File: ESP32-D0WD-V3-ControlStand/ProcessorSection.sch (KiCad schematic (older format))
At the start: 31 parts

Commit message: Nearly complete schematic.  Added Antenna footprint.
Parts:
- removed J?: Programming Header, Pin_Headers:Pin_Header_Straight_2x03_Pitch2.54mm, symbol Conn_02x03_Odd_Even
- added AE?: Antenna_Shield, Antenna:Antenna, symbol Antenna_Shield
- added C? (x2): 270pf, Capacitors_SMD:C_0402, symbol C_Small
- added C? (x2): 47pf, Capacitors_SMD:C_0402, symbol C_Small
- added C?: 10pf, Capacitors_SMD:C_0402, symbol C_Small
- added C? (x2): 100nf, Capacitors_SMD:C_0402, symbol C_Small
- added C?: 4.7uf, Capacitors_SMD:CP_Elec_4x5.7, symbol CP1_Small
- added C?: 5.8pf, Capacitors_SMD:C_0402, symbol C_Small
- added J?: USB_OTG, Connectors_USB:USB_Micro-B_Molex_47346-0001, symbol USB_OTG
- added L? (x2): Ferrite Bead, Inductors_SMD:L_0402, symbol Ferrite_Bead_Small
- added Q? (x2): UMH3N, TO_SOT_Packages_SMD:SOT-363_SC-70-6, symbol UMH3N
- added R? (x2): 27, Resistors_SMD:R_0402, symbol R
- added U?: FT231XS-R, Housings_SSOP:SSOP-20_5.3x7.2mm_Pitch0.65mm, symbol FT231XS-R
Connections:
- net labels added: 0, 12, 16, 17, 18, 19, 23, 25, 26, 27, 32, 33, 34, 35, Antenna, DTR, RTS, Reset, VBUS, VN, VP
- net labels removed: GPIO0(Buttons1), GPIO12(Points1), GPIO13(Points2), GPIO14(Points3), GPIO16(Buttons4), GPIO17(LEDS1), GPIO18(LEDS2), GPIO19(LEDS3), GPIO23(LEDS4), GPIO25(Motor1), GPIO26(Motor2), GPIO27(Points4), GPIO32(Motor3), GPIO33(Motor4), GPIO34(OD1), GPIO35(OD2), GPIO36(OD3), GPIO37(Buttons3), GPIO38(Buttons2), GPIO39(OD4)
- wire segments 91 -> 140
- no-connect marks 1 -> 8

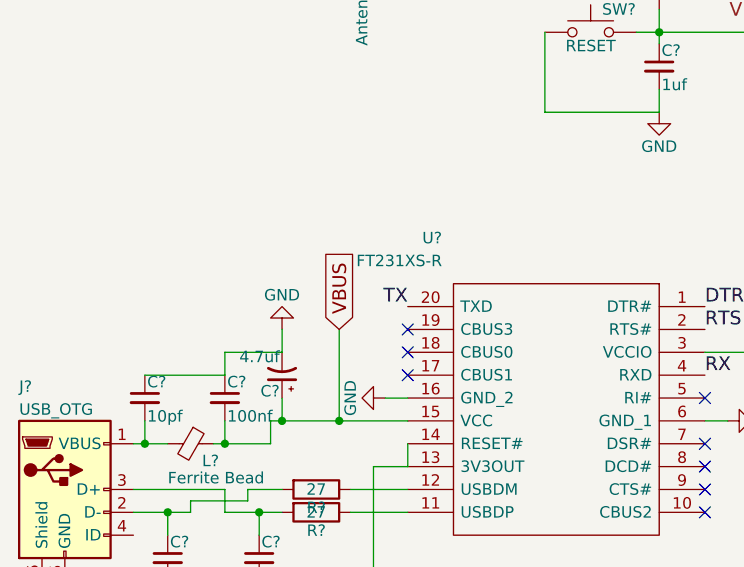
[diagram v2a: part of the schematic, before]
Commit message: Complete PS, work on parts spec.
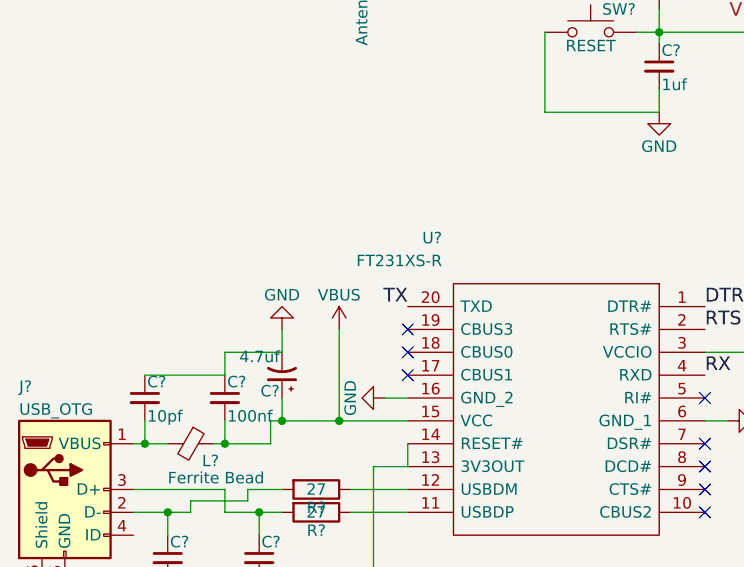
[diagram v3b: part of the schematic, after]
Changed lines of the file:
@@
 LIBS:ESP32-D0WD-V3
 LIBS:W25Q32JVSSIQ
+LIBS:mcp73871
+LIBS:lm2574n-5
 LIBS:ESP32-D0WD-V3-ControlStand-cache
 EELAYER 25 0
@@
 Wire Wire Line
 	3100 6850 3100 7000
-Text GLabel 2250 5300 1    60   Input ~ 0
-VBUS
 Wire Wire Line
 	2250 5300 2250 5700
@@
 Wire Wire Line
 	2650 3300 2650 3350
+$Comp
+L VBUS #PWR?
+U 1 1 62E2A6A1
+P 2250 5300
+F 0 "#PWR?" H 2250 5150 50  0001 C CNN
+F 1 "VBUS" H 2250 5450 50  0000 C CNN
+F 2 "" H 2250 5300 50  0001 C CNN
+F 3 "" H 2250 5300 50  0001 C CNN
+	1    2250 5300
+	1    0    0    -1
+$EndComp
 $EndSCHEMATC

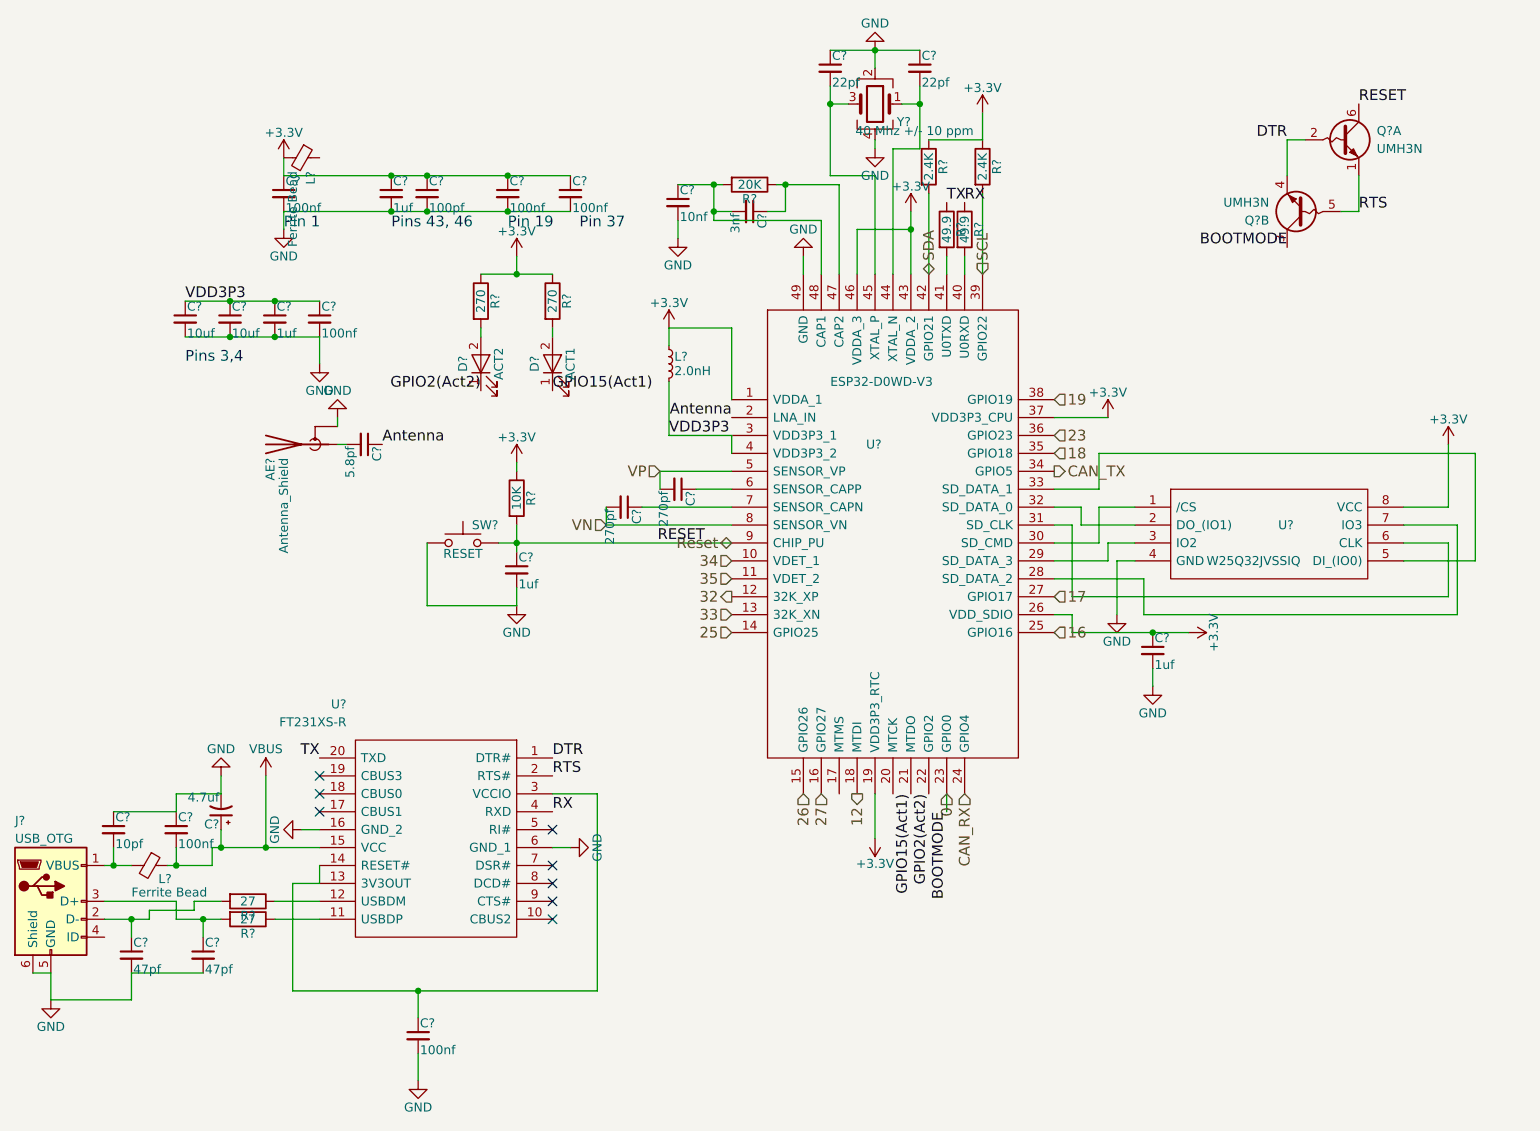
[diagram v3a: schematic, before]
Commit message: Completed parts spec for ESP32-D0WD-V3-ControlStand.
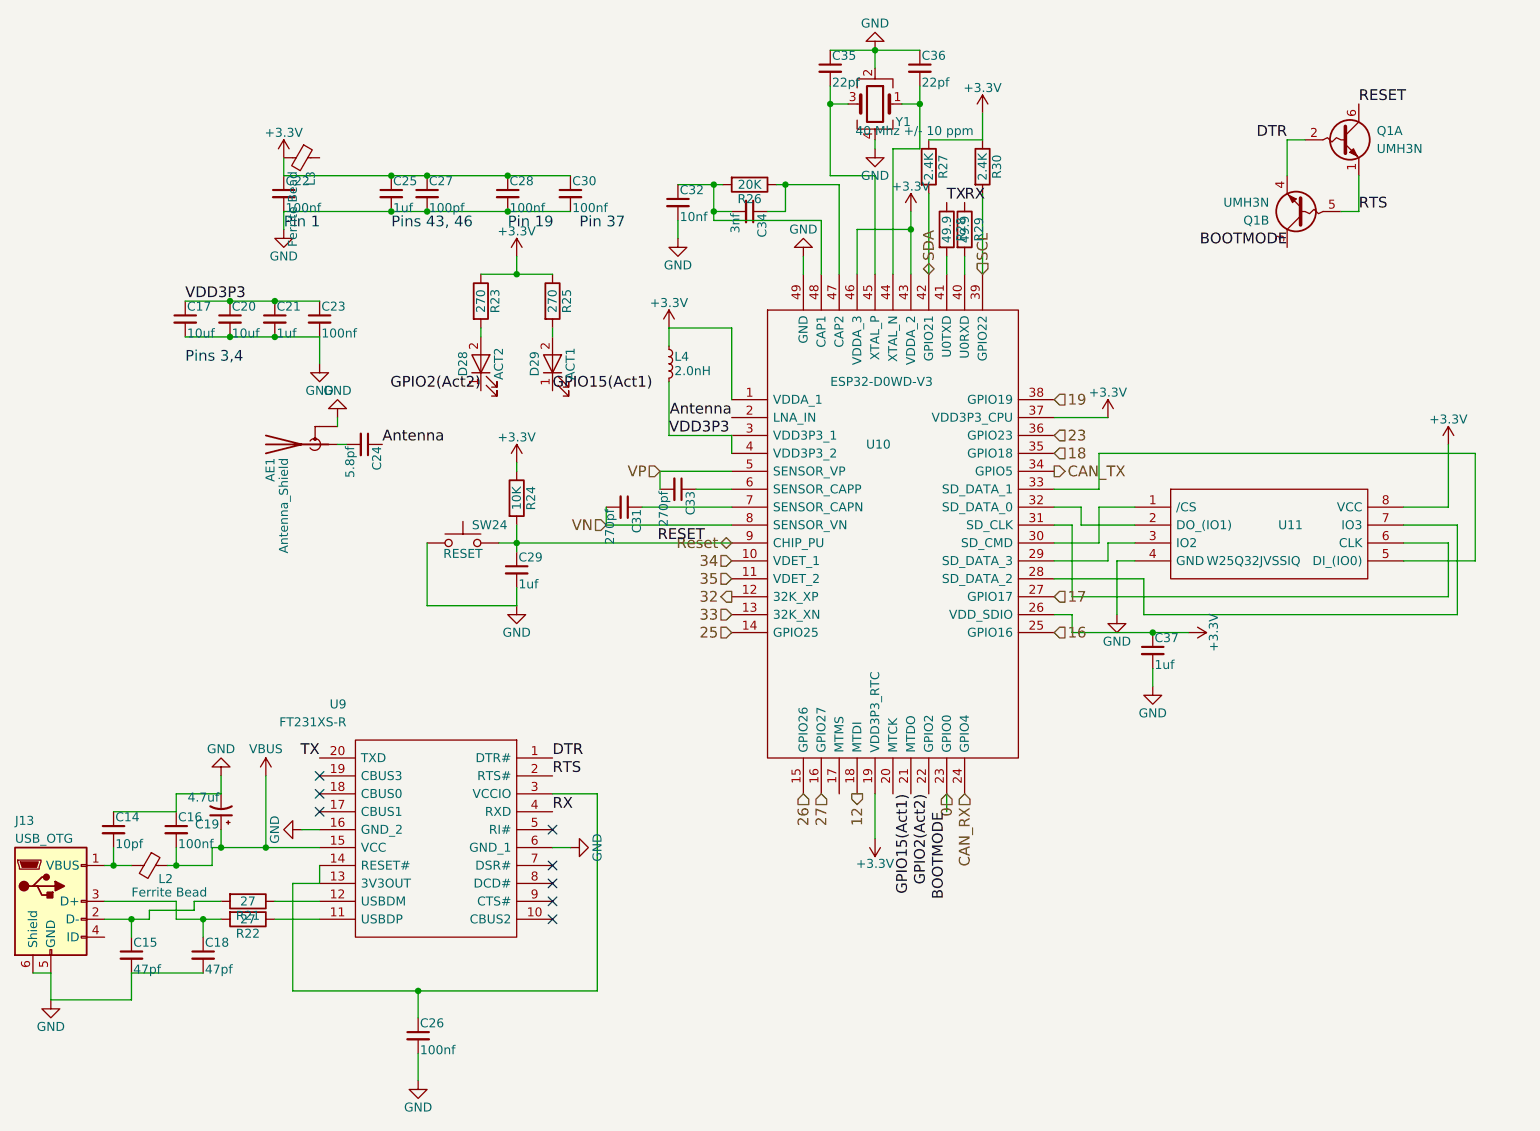
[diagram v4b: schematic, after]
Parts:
- gave numbers to parts that had none: 47

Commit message: Working on the PCB Layout.
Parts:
- removed L3: Ferrite Bead, Inductors_SMD:L_0402, symbol Ferrite_Bead_Small
- added MK17, MK18, MK19: Mounting_Hole, Mounting_Holes:MountingHole_2.5mm, symbol Mounting_Hole
- added MK20: Mounting_Hole_PAD, Mounting_Holes:MountingHole_2.5mm_Pad, symbol Mounting_Hole_PAD
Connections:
- no-connect marks 8 -> 9
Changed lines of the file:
@@
 LIBS:mcp73871
 LIBS:lm2574n-5
+LIBS:mechanical
+LIBS:graphic_symbols
 LIBS:ESP32-D0WD-V3-ControlStand-cache
 EELAYER 25 0
@@
 $EndComp
 $Comp
-L +3.3V #PWR85
+L +3.3V #PWR060
 U 1 1 62DF2387
 P 8850 3450
-F 0 "#PWR85" H 8850 3300 50  0001 C CNN
+F 0 "#PWR060" H 8850 3300 50  0001 C CNN
 F 1 "+3.3V" H 8850 3590 50  0000 C CNN
 F 2 "" H 8850 3450 50  0001 C CNN
@@
 $EndComp
 $Comp
-L GND #PWR82
+L GND #PWR061
 U 1 1 62DF2388
 P 7000 4400
-F 0 "#PWR82" H 7000 4150 50  0001 C CNN
+F 0 "#PWR061" H 7000 4150 50  0001 C CNN
 F 1 "GND" H 7000 4250 50  0000 C CNN
 F 2 "" H 7000 4400 50  0001 C CNN
@@
 $EndComp
 $Comp
-L GND #PWR71
+L GND #PWR062
 U 1 1 62DF2391
 P 3650 4350
-F 0 "#PWR71" H 3650 4100 50  0001 C CNN
+F 0 "#PWR062" H 3650 4100 50  0001 C CNN
 F 1 "GND" H 3650 4200 50  0000 C CNN
 F 2 "" H 3650 4350 50  0001 C CNN
@@
 $EndComp
 $Comp
-L +3.3V #PWR70
+L +3.3V #PWR063
 U 1 1 62DF2392
 P 3650 3550
-F 0 "#PWR70" H 3650 3400 50  0001 C CNN
+F 0 "#PWR063" H 3650 3400 50  0001 C CNN
 F 1 "+3.3V" H 3650 3690 50  0000 C CNN
 F 2 "" H 3650 3550 50  0001 C CNN
@@
 $EndComp
 $Comp
-L GND #PWR83
+L GND #PWR064
 U 1 1 62DF2394
 P 7200 4800
-F 0 "#PWR83" H 7200 4550 50  0001 C CNN
+F 0 "#PWR064" H 7200 4550 50  0001 C CNN
 F 1 "GND" H 7200 4650 50  0000 C CNN
 F 2 "" H 7200 4800 50  0001 C CNN
@@
 $EndComp
 $Comp
-L +3.3V #PWR84
+L +3.3V #PWR065
 U 1 1 62DF2395
 P 7400 4500
-F 0 "#PWR84" H 7400 4350 50  0001 C CNN
+F 0 "#PWR065" H 7400 4350 50  0001 C CNN
 F 1 "+3.3V" H 7400 4640 50  0000 C CNN
 F 2 "" H 7400 4500 50  0001 C CNN
@@
 $EndComp
 $Comp
-L +3.3V #PWR73
+L +3.3V #PWR066
 U 1 1 62DF2397
 P 4500 2800
-F 0 "#PWR73" H 4500 2650 50  0001 C CNN
+F 0 "#PWR066" H 4500 2650 50  0001 C CNN
 F 1 "+3.3V" H 4500 2940 50  0000 C CNN
 F 2 "" H 4500 2800 50  0001 C CNN
@@
 $EndComp
 $Comp
-L +3.3V #PWR81
+L +3.3V #PWR067
 U 1 1 62DF2398
 P 6950 3300
-F 0 "#PWR81" H 6950 3150 50  0001 C CNN
+F 0 "#PWR067" H 6950 3150 50  0001 C CNN
 F 1 "+3.3V" H 6950 3440 50  0000 C CNN
 F 2 "" H 6950 3300 50  0001 C CNN
@@
 $EndComp
 $Comp
-L +3.3V #PWR79
+L +3.3V #PWR068
 U 1 1 62DF2399
 P 5850 2150
-F 0 "#PWR79" H 5850 2000 50  0001 C CNN
+F 0 "#PWR068" H 5850 2000 50  0001 C CNN
 F 1 "+3.3V" H 5850 2290 50  0000 C CNN
 F 2 "" H 5850 2150 50  0001 C CNN
@@
 $EndComp
 $Comp
-L +3.3V #PWR78
+L +3.3V #PWR069
 U 1 1 62DF239A
 P 5650 5650
-F 0 "#PWR78" H 5650 5500 50  0001 C CNN
+F 0 "#PWR069" H 5650 5500 50  0001 C CNN
 F 1 "+3.3V" H 5650 5790 50  0000 C CNN
 F 2 "" H 5650 5650 50  0001 C CNN
@@
 VDD3P3
 $Comp
-L GND #PWR75
+L GND #PWR070
 U 1 1 62DF239B
 P 5250 2400
-F 0 "#PWR75" H 5250 2150 50  0001 C CNN
+F 0 "#PWR070" H 5250 2150 50  0001 C CNN
 F 1 "GND" H 5250 2250 50  0000 C CNN
 F 2 "" H 5250 2400 50  0001 C CNN
@@
 	5400 1550 5500 1550
 $Comp
-L GND #PWR77
+L GND #PWR071
 U 1 1 62DF239D
 P 5650 1800
-F 0 "#PWR77" H 5650 1550 50  0001 C CNN
+F 0 "#PWR071" H 5650 1550 50  0001 C CNN
 F 1 "GND" H 5650 1650 50  0000 C CNN
 F 2 "" H 5650 1800 50  0001 C CNN
@@
 $EndComp
 $Comp
-L GND #PWR76
+L GND #PWR072
 U 1 1 62DF239E
 P 5650 1250
-F 0 "#PWR76" H 5650 1000 50  0001 C CNN
+F 0 "#PWR072" H 5650 1000 50  0001 C CNN
 F 1 "GND" H 5650 1100 50  0000 C CNN
 F 2 "" H 5650 1250 50  0001 C CNN
@@
 Connection ~ 4750 2150
 $Comp
-L GND #PWR74
+L GND #PWR073
 U 1 1 62DF23A4
 P 4550 2300
-F 0 "#PWR74" H 4550 2050 50  0001 C CNN
+F 0 "#PWR073" H 4550 2050 50  0001 C CNN
 F 1 "GND" H 4550 2150 50  0000 C CNN
 F 2 "" H 4550 2300 50  0001 C CNN
@@
 Connection ~ 2050 2850
 $Comp
-L GND #PWR66
+L GND #PWR074
 U 1 1 62DF23A9
 P 2550 3000
-F 0 "#PWR66" H 2550 2750 50  0001 C CNN
+F 0 "#PWR074" H 2550 2750 50  0001 C CNN
 F 1 "GND" H 2550 2850 50  0000 C CNN
 F 2 "" H 2550 3000 50  0001 C CNN
@@
 Connection ~ 2950 2150
 $Comp
-L +3.3V #PWR63
+L +3.3V #PWR075
 U 1 1 62DF23AF
 P 2350 1850
-F 0 "#PWR63" H 2350 1700 50  0001 C CNN
+F 0 "#PWR075" H 2350 1700 50  0001 C CNN
 F 1 "+3.3V" H 2350 1990 50  0000 C CNN
 F 2 "" H 2350 1850 50  0001 C CNN
@@
 $EndComp
 $Comp
-L GND #PWR64
+L GND #PWR076
 U 1 1 62DF23B0
 P 2350 2250
-F 0 "#PWR64" H 2350 2000 50  0001 C CNN
+F 0 "#PWR076" H 2350 2000 50  0001 C CNN
 F 1 "GND" H 2350 2100 50  0000 C CNN
 F 2 "" H 2350 2250 50  0001 C CNN
@@
 	5950 1750 6250 1750
 $Comp
-L +3.3V #PWR80
+L +3.3V #PWR077
 U 1 1 62DF23B3
 P 6250 1600
-F 0 "#PWR80" H 6250 1450 50  0001 C CNN
+F 0 "#PWR077" H 6250 1450 50  0001 C CNN
 F 1 "+3.3V" H 6250 1740 50  0000 C CNN
 F 2 "" H 6250 1600 50  0001 C CNN
@@
 $EndComp
 $Comp
-L +3.3V #PWR69
+L +3.3V #PWR078
 U 1 1 62DF23B8
 P 3650 2400
-F 0 "#PWR69" H 3650 2250 50  0001 C CNN
+F 0 "#PWR078" H 3650 2250 50  0001 C CNN
 F 1 "+3.3V" H 3650 2540 50  0000 C CNN
 F 2 "" H 3650 2400 50  0001 C CNN
@@
 $EndComp
 $Comp
-L Ferrite_Bead_Small L3
-U 1 1 62E118FA
-P 2450 1850
-F 0 "L3" H 2525 1900 50  0000 L CNN
-F 1 "Ferrite Bead" H 2525 1800 50  0000 L CNN
-F 2 "Inductors_SMD:L_0402" V 2380 1850 50  0001 C CNN
-F 3 "" H 2450 1850 50  0001 C CNN
-F 4 "810-MMZ1005S800CTD25" H 2450 1850 60  0001 C CNN "Mouser Part Number"
-	1    2450 1850
-	0    1    1    0
-$EndComp
-$Comp
 L UMH3N Q1
 U 1 1 62E11915
@@
 NoConn ~ 3850 6000
 $Comp
-L GND #PWR72
+L GND #PWR079
 U 1 1 62E17368
 P 3950 5700
-F 0 "#PWR72" H 3950 5450 50  0001 C CNN
+F 0 "#PWR079" H 3950 5450 50  0001 C CNN
 F 1 "GND" H 3950 5550 50  0000 C CNN
 F 2 "" H 3950 5700 50  0001 C CNN
@@
 NoConn ~ 2550 5300
 $Comp
-L GND #PWR65
+L GND #PWR080
 U 1 1 62E179B5
 P 2450 5600
-F 0 "#PWR65" H 2450 5350 50  0001 C CNN
+F 0 "#PWR080" H 2450 5350 50  0001 C CNN
 F 1 "GND" H 2450 5450 50  0000 C CNN
 F 2 "" H 2450 5600 50  0001 C CNN
@@
 	950  6400 1050 6400
 $Comp
-L GND #PWR60
+L GND #PWR081
 U 1 1 62E187A2
 P 1050 6550
-F 0 "#PWR60" H 1050 6300 50  0001 C CNN
+F 0 "#PWR081" H 1050 6300 50  0001 C CNN
 F 1 "GND" H 1050 6400 50  0000 C CNN
 F 2 "" H 1050 6550 50  0001 C CNN
@@
 	1750 5400 2000 5400
 $Comp
-L GND #PWR61
+L GND #PWR082
 U 1 1 62E1A0F6
 P 2000 5300
-F 0 "#PWR61" H 2000 5050 50  0001 C CNN
+F 0 "#PWR082" H 2000 5050 50  0001 C CNN
 F 1 "GND" H 2000 5150 50  0000 C CNN
 F 2 "" H 2000 5300 50  0001 C CNN
@@
 Connection ~ 3100 6500
 $Comp
-L GND #PWR68
+L GND #PWR083
 U 1 1 62E1A448
 P 3100 7000
-F 0 "#PWR68" H 3100 6750 50  0001 C CNN
+F 0 "#PWR083" H 3100 6750 50  0001 C CNN
 F 1 "GND" H 3100 6850 50  0000 C CNN
 F 2 "" H 3100 7000 50  0001 C CNN
@@
 	2700 3450 2650 3450
 $Comp
-L GND #PWR67
+L GND #PWR084
 U 1 1 62E1EC1A
 P 2650 3300
-F 0 "#PWR67" H 2650 3050 50  0001 C CNN
+F 0 "#PWR084" H 2650 3050 50  0001 C CNN
 F 1 "GND" H 2650 3150 50  0000 C CNN
 F 2 "" H 2650 3300 50  0001 C CNN
@@
 	2650 3300 2650 3350
 $Comp
-L VBUS #PWR62
+L VBUS #PWR085
 U 1 1 62E2A6A1
 P 2250 5300
-F 0 "#PWR62" H 2250 5150 50  0001 C CNN
+F 0 "#PWR085" H 2250 5150 50  0001 C CNN
 F 1 "VBUS" H 2250 5450 50  0000 C CNN
 F 2 "" H 2250 5300 50  0001 C CNN
@@
 	1    0    0    -1
 $EndComp
+$Comp
+L Mounting_Hole MK17
+U 1 1 62E6E1A3
+P 7500 5350
+F 0 "MK17" H 7500 5550 50  0000 C CNN
+F 1 "Mounting_Hole" H 7500 5475 50  0000 C CNN
+F 2 "Mounting_Holes:MountingHole_2.5mm" H 7500 5350 50  0001 C CNN
+F 3 "" H 7500 5350 50  0001 C CNN
+	1    7500 5350
+	1    0    0    -1
+$EndComp
+$Comp
+L Mounting_Hole MK18
+U 1 1 62E6E22C
+P 7850 5300
+F 0 "MK18" H 7850 5500 50  0000 C CNN
+F 1 "Mounting_Hole" H 7850 5425 50  0000 C CNN
+F 2 "Mounting_Holes:MountingHole_2.5mm" H 7850 5300 50  0001 C CNN
+F 3 "" H 7850 5300 50  0001 C CNN
+	1    7850 5300
+	1    0    0    -1
+$EndComp
+$Comp
+L Mounting_Hole MK19
+U 1 1 62E6E2A3
+P 8300 5250
+F 0 "MK19" H 8300 5450 50  0000 C CNN
+F 1 "Mounting_Hole" H 8300 5375 50  0000 C CNN
+F 2 "Mounting_Holes:MountingHole_2.5mm" H 8300 5250 50  0001 C CNN
+F 3 "" H 8300 5250 50  0001 C CNN
+	1    8300 5250
+	1    0    0    -1
+$EndComp
+$Comp
+L Mounting_Hole_PAD MK20
+U 1 1 62E6E35E
+P 8850 5300
+F 0 "MK20" H 8850 5550 50  0000 C CNN
+F 1 "Mounting_Hole_PAD" H 8850 5475 50  0000 C CNN
+F 2 "Mounting_Holes:MountingHole_2.5mm_Pad" H 8850 5300 50  0001 C CNN
+F 3 "" H 8850 5300 50  0001 C CNN
+	1    8850 5300
+	1    0    0    -1
+$EndComp
+NoConn ~ 5450 5400
 $EndSCHEMATC
